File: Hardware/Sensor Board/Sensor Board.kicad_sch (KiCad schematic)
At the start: 3 parts, among them J1 68610414422, U1 HTU21DF

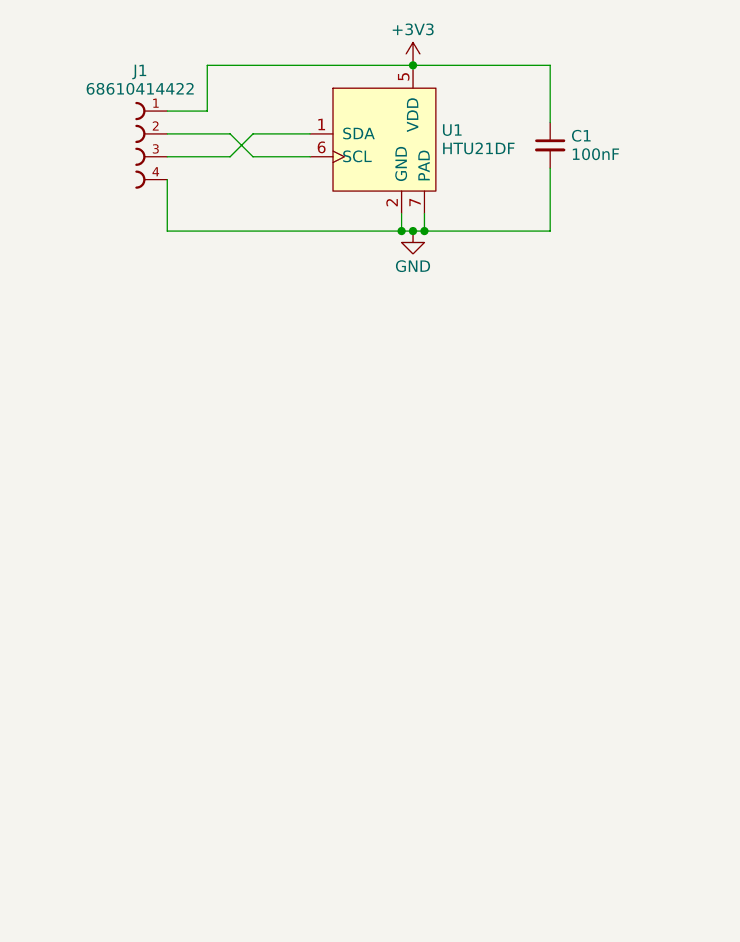
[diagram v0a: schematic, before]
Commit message: Created Switch Board PCB Project
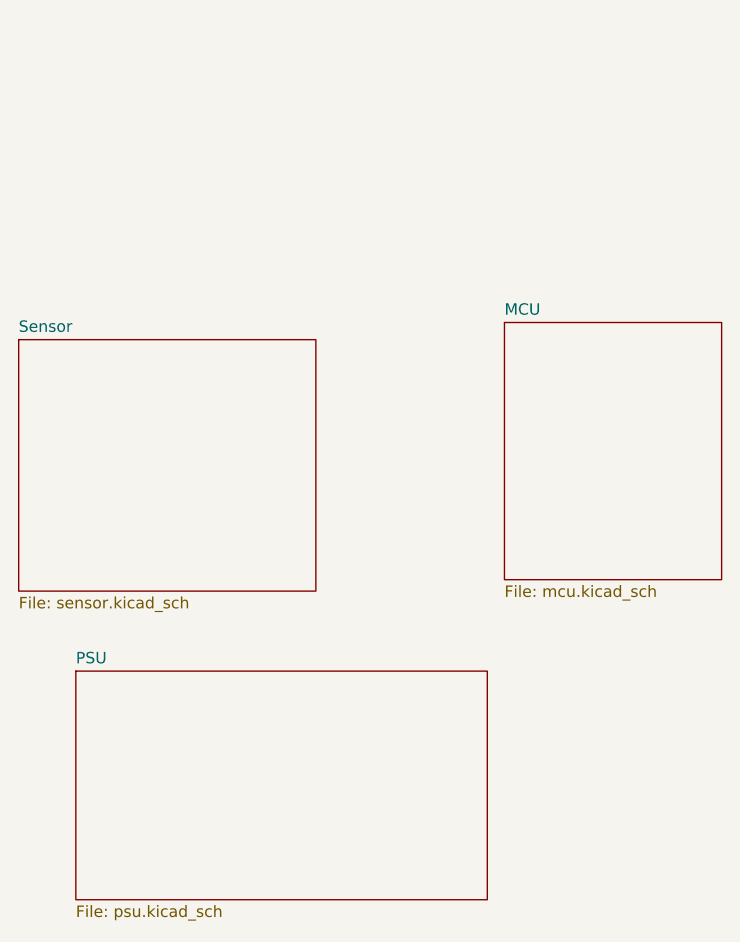
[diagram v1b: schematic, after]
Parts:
- removed C1: 100nF, Capacitor_SMD:C_0402_1005Metric, symbol Device:C_Small
- removed J1: 68610414422, manul_tech:68610414422, symbol manul_tech:68610414422
- removed U1: HTU21DF, manul_tech:HTU21DF, symbol manul_tech:HTU21DF
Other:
- added sheet MCU (mcu.kicad_sch)
- added sheet PSU (psu.kicad_sch)
- added sheet Sensor (sensor.kicad_sch)
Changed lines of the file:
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@@
 (kicad_sch (version 20230121) (generator eeschema)
   (paper "A4")
-  (junction (at 116.84 67.31) (diameter 0) (color 0 0 0 0)
-  )
-  (junction (at 115.57 85.725) (diameter 0) (color 0 0 0 0)
-  )
-  (junction (at 118.11 85.725) (diameter 0) (color 0 0 0 0)
-  )
-  (junction (at 116.84 85.725) (diameter 0) (color 0 0 0 0)
-  )
-  (wire (pts (xy 132.08 73.66) (xy 132.08 67.31))
-    (stroke (width 0) (type default))
-  )
-  (wire (pts (xy 96.52 77.47) (xy 99.06 74.93))
-    (stroke (width 0) (type default))
-  )
-  (wire (pts (xy 118.11 85.725) (xy 116.84 85.725))
-    (stroke (width 0) (type default))
-  )
-  (wire (pts (xy 118.11 83.82) (xy 118.11 85.725))
-    (stroke (width 0) (type default))
-  )
-  (wire (pts (xy 116.84 67.31) (xy 132.08 67.31))
-    (stroke (width 0) (type default))
-  )
-  (wire (pts (xy 115.57 85.725) (xy 116.84 85.725))
-    (stroke (width 0) (type default))
-  )
-  (wire (pts (xy 96.52 74.93) (xy 99.06 77.47))
-    (stroke (width 0) (type default))
-  )
-  (wire (pts (xy 93.98 72.39) (xy 93.98 67.31))
-    (stroke (width 0) (type default))
-  )
-  (wire (pts (xy 132.08 78.74) (xy 132.08 85.725))
-    (stroke (width 0) (type default))
-  )
-  (wire (pts (xy 89.535 85.725) (xy 115.57 85.725))
-    (stroke (width 0) (type default))
-  )
-  (wire (pts (xy 96.52 77.47) (xy 89.535 77.47))
-    (stroke (width 0) (type default))
-  )
-  (wire (pts (xy 89.535 74.93) (xy 96.52 74.93))
-    (stroke (width 0) (type default))
-  )
-  (wire (pts (xy 89.535 72.39) (xy 93.98 72.39))
-    (stroke (width 0) (type default))
-  )
-  (wire (pts (xy 105.41 74.93) (xy 99.06 74.93))
-    (stroke (width 0) (type default))
-  )
-  (wire (pts (xy 93.98 67.31) (xy 116.84 67.31))
-    (stroke (width 0) (type default))
-  )
-  (wire (pts (xy 132.08 85.725) (xy 118.11 85.725))
-    (stroke (width 0) (type default))
-  )
-  (wire (pts (xy 99.06 77.47) (xy 105.41 77.47))
-    (stroke (width 0) (type default))
-  )
-  (wire (pts (xy 89.535 80.01) (xy 89.535 85.725))
-    (stroke (width 0) (type default))
-  )
-  (wire (pts (xy 115.57 83.82) (xy 115.57 85.725))
-    (stroke (width 0) (type default))
-  )
-  (symbol (lib_id "Device:C_Small") (at 132.08 76.2 0) (unit 1)
-    (in_bom yes) (on_board yes) (dnp no) (fields_autoplaced)
-    (property "Reference" "C1" (at 134.4041 75.1823 0)
-      (effects (font (size 1.27 1.27)) (justify left))
+  (sheet (at 73.025 97.79) (size 33.02 27.94) (fields_autoplaced)
+    (stroke (width 0.1524) (type solid))
+    (fill (color 0 0 0 0.0000))
+    (property "Sheetname" "Sensor" (at 73.025 97.0784 0)
+      (effects (font (size 1.27 1.27)) (justify left bottom))
     )
-    (property "Value" "100nF" (at 134.4041 77.2303 0)
-      (effects (font (size 1.27 1.27)) (justify left))
+    (property "Sheetfile" "sensor.kicad_sch" (at 73.025 126.3146 0)
+      (effects (font (size 1.27 1.27)) (justify left top))
     )
-    (property "Footprint" "Capacitor_SMD:C_0402_1005Metric" (at 132.08 76.2 0)
-      (effects (font (size 1.27 1.27)) hide)
-    )
-    (property "Datasheet" "~" (at 132.08 76.2 0)
-      (effects (font (size 1.27 1.27)) hide)
-    )
-    (pin "1")
-    (pin "2")
     (instances
       (project "Sensor Board"
-        (path "/4124114b-a393-44c3-a32c-68658c8fd741"
-          (reference "C1") (unit 1)
-        )
+        (path "/4124114b-a393-44c3-a32c-68658c8fd741" (page "2"))
       )
     )
   )
-  (symbol (lib_id "manul_tech:HTU21DF") (at 116.84 69.85 0) (unit 1)
-    (in_bom yes) (on_board yes) (dnp no) (fields_autoplaced)
-    (property "Reference" "U1" (at 120.015 74.541 0)
-      (effects (font (size 1.27 1.27)) (justify left))
+  (sheet (at 127 95.885) (size 24.13 28.575) (fields_autoplaced)
+    (stroke (width 0.1524) (type solid))
+    (fill (color 0 0 0 0.0000))
+    (property "Sheetname" "MCU" (at 127 95.1734 0)
+      (effects (font (size 1.27 1.27)) (justify left bottom))
     )
-    (property "Value" "HTU21DF" (at 120.015 76.589 0)
-      (effects (font (size 1.27 1.27)) (justify left))
+    (property "Sheetfile" "mcu.kicad_sch" (at 127 125.0446 0)
+      (effects (font (size 1.27 1.27)) (justify left top))
     )
-    (property "Footprint" "manul_tech:HTU21DF" (at 115.57 60.96 0)
-      (effects (font (size 1.27 1.27)) hide)
-    )
-    (property "Datasheet" "https://cdn-shop.adafruit.com/datasheets/1899_HTU21D.pdf" (at 115.57 60.96 0)
-      (effects (font (size 1.27 1.27)) hide)
-    )
-    (pin "1")
-    (pin "2")
-    (pin "5")
-    (pin "6")
-    (pin "7")
     (instances
       (project "Sensor Board"
-        (path "/4124114b-a393-44c3-a32c-68658c8fd741"
-          (reference "U1") (unit 1)
-        )
+        (path "/4124114b-a393-44c3-a32c-68658c8fd741" (page "3"))
       )
     )
   )
-  (symbol (lib_id "power:+3V3") (at 116.84 67.31 0) (unit 1)
-    (in_bom yes) (on_board yes) (dnp no) (fields_autoplaced)
-    (property "Reference" "#PWR02" (at 116.84 71.12 0)
-      (effects (font (size 1.27 1.27)) hide)
+  (sheet (at 79.375 134.62) (size 45.72 25.4) (fields_autoplaced)
+    (stroke (width 0.1524) (type solid))
+    (fill (color 0 0 0 0.0000))
+    (property "Sheetname" "PSU" (at 79.375 133.9084 0)
+      (effects (font (size 1.27 1.27)) (justify left bottom))
     )
-    (property "Value" "+3V3" (at 116.84 63.365 0)
-      (effects (font (size 1.27 1.27)))
+    (property "Sheetfile" "psu.kicad_sch" (at 79.375 160.6046 0)
+      (effects (font (size 1.27 1.27)) (justify left top))
     )
-    (property "Footprint" "" (at 116.84 67.31 0)
-      (effects (font (size 1.27 1.27)) hide)
-    )
-    (property "Datasheet" "" (at 116.84 67.31 0)
-      (effects (font (size 1.27 1.27)) hide)
-    )
-    (pin "1")
     (instances
       (project "Sensor Board"
-        (path "/4124114b-a393-44c3-a32c-68658c8fd741"
-          (reference "#PWR02") (unit 1)
-        )
+        (path "/4124114b-a393-44c3-a32c-68658c8fd741" (page "4"))
       )
     )
-  )
-  (symbol (lib_id "power:GND") (at 116.84 85.725 0) (unit 1)
-    (in_bom yes) (on_board yes) (dnp no) (fields_autoplaced)
-    (property "Reference" "#PWR01" (at 116.84 92.075 0)
-      (effects (font (size 1.27 1.27)) hide)
-    )
-    (property "Value" "GND" (at 116.84 89.67 0)
-      (effects (font (size 1.27 1.27)))
-    )
-    (property "Footprint" "" (at 116.84 85.725 0)
-      (effects (font (size 1.27 1.27)) hide)
-    )
-    (property "Datasheet" "" (at 116.84 85.725 0)
-      (effects (font (size 1.27 1.27)) hide)
-    )
-    (pin "1")
-    (instances
-      (project "Sensor Board"
-        (path "/4124114b-a393-44c3-a32c-68658c8fd741"
-          (reference "#PWR01") (unit 1)
-        )
-      )
-    )
-  )
-  (symbol (lib_id "manul_tech:68610414422") (at 84.455 74.93 180) (unit 1)
-    (in_bom yes) (on_board yes) (dnp no) (fields_autoplaced)
-    (property "Reference" "J1" (at 86.5486 67.921 0)
-      (effects (font (size 1.27 1.27)))
-    )
-    (property "Value" "68610414422" (at 86.5486 69.969 0)
-      (effects (font (size 1.27 1.27)))
-    )
-    (property "Footprint" "manul_tech:68610414422" (at 84.455 74.93 0)
-      (effects (font (size 1.27 1.27)) (justify bottom) hide)
-    )
-    (property "Datasheet" "" (at 84.455 74.93 0)
-      (effects (font (size 1.27 1.27)) hide)
-    )
-    (property "internalRef" "" (at 84.455 74.93 0)
-      (effects (font (size 1.27 1.27)) hide)
-    )
-    (property "Manufacturer" "Wuerth Elektronik" (at 84.455 74.93 0)
-      (effects (font (size 1.27 1.27)) hide)
-    )
-    (property "MPN" "68610414422" (at 84.455 74.93 0)
-      (effects (font (size 1.27 1.27)) hide)
-    )
-    (pin "1")
-    (pin "2")
-    (pin "3")
-    (pin "4")
-    (instances
-      (project "Sensor Board"
-        (path "/4124114b-a393-44c3-a32c-68658c8fd741"
-          (reference "J1") (unit 1)
-        )
-      )
-    )
